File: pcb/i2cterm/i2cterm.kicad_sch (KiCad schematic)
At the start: 8 parts, among them J1 GROVE VERTICAL, J2 GROVE VERTICAL

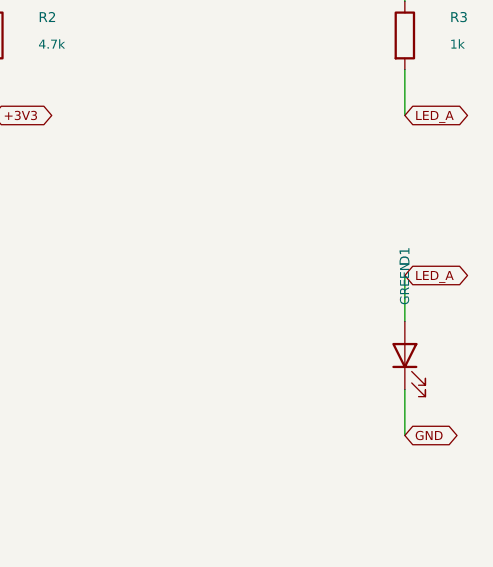
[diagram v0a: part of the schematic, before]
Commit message: Use the basic-library red LED C2286 on the i2cterm board
D1 moves from the extended KT-0603YG green LED (C2289) to the KT-0603R red
LED (C2286), a JLCPCB basic part from the same KENTO 0603 family, which
avoids the extended-part fee. The footprint and the 1k resistor stay; the
current rises from about 1.2 to 1.4 mA. The JLCPCB assembly preview shows
the cathode on the GND pad.

Co-Authored-By: Claude Opus 5.5 <noreply@anthropic.com>
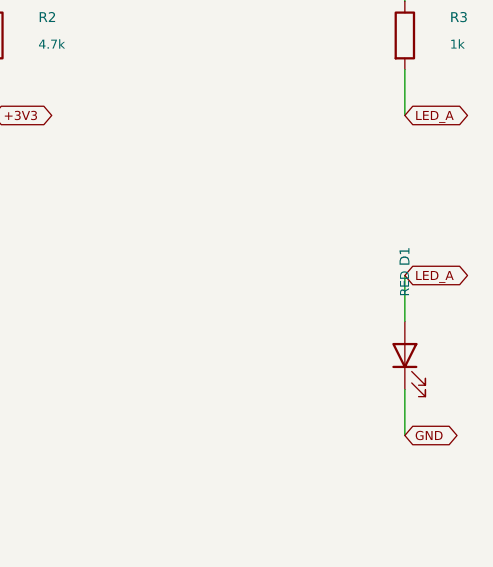
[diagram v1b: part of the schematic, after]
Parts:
- D1: value GREEN -> RED; LCSC C2289 -> C2286; MPN KT-0603YG -> KT-0603R
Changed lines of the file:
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@@
 (wire (pts (xy 185.42 76.2) (xy 185.42 71.12)) (stroke (width 0) (type default)))
 (global_label "LED_A" (shape bidirectional) (at 185.42 71.12 0) (effects (font (size 1.0 1.0)) (justify left)) (property "Intersheetrefs" "${INTERSHEET_REFS}" (at 185.42 71.12 0) (hide yes) (effects (font (size 1.0 1.0)))))
-(symbol (lib_id "Device:LED") (at 185.42 80.01 90) (unit 1) (exclude_from_sim no) (in_bom yes) (on_board yes) (dnp no) (property "Reference" "D1" (at 185.42 69.01 0) (effects (font (size 1.1 1.1)))) (property "Value" "GREEN" (at 185.42 72.01 0) (effects (font (size 1.0 1.0)))) (property "Footprint" "LED_SMD:LED_0603_1608Metric" (at 185.42 80.01 0) (effects (font (size 1.0 1.0))) (hide yes)) (property "Datasheet" "" (at 185.42 80.01 0) (effects (font (size 1.0 1.0))) (hide yes)) (property "Description" "Light emitting diode" (at 185.42 80.01 0) (effects (font (size 1.0 1.0))) (hide yes)) (property "MPN" "KT-0603YG" (at 185.42 80.01 0) (effects (font (size 1.0 1.0))) (hide yes)) (pin "1") (pin "2") (instances (project "i2cterm" (path "/f4c31e8a-4653-5df7-a27a-ec98410162ff" (reference "D1") (unit 1)))) (property "LCSC" "C2289" (at 185.42 80.01 0) (effects (font (size 1 1))) (hide yes)))
+(symbol (lib_id "Device:LED") (at 185.42 80.01 90) (unit 1) (exclude_from_sim no) (in_bom yes) (on_board yes) (dnp no) (property "Reference" "D1" (at 185.42 69.01 0) (effects (font (size 1.1 1.1)))) (property "Value" "RED" (at 185.42 72.01 0) (effects (font (size 1.0 1.0)))) (property "Footprint" "LED_SMD:LED_0603_1608Metric" (at 185.42 80.01 0) (effects (font (size 1.0 1.0))) (hide yes)) (property "Datasheet" "" (at 185.42 80.01 0) (effects (font (size 1.0 1.0))) (hide yes)) (property "Description" "Light emitting diode" (at 185.42 80.01 0) (effects (font (size 1.0 1.0))) (hide yes)) (property "MPN" "KT-0603R" (at 185.42 80.01 0) (effects (font (size 1.0 1.0))) (hide yes)) (pin "1") (pin "2") (instances (project "i2cterm" (path "/f4c31e8a-4653-5df7-a27a-ec98410162ff" (reference "D1") (unit 1)))) (property "LCSC" "C2286" (at 185.42 80.01 0) (effects (font (size 1 1))) (hide yes)))
 (symbol (lib_id "Mechanical:MountingHole") (at 44.45 110.49 0) (unit 1) (exclude_from_sim no) (in_bom no) (on_board yes) (dnp no) (property "Reference" "H1" (at 49.45 108.49 0) (effects (font (size 1.1 1.1)) (justify left))) (property "Value" "M2.5" (at 49.45 111.49 0) (effects (font (size 1.0 1.0)) (justify left))) (property "Footprint" "MountingHole:MountingHole_2.7mm_M2.5" (at 44.45 110.49 0) (effects (font (size 1.0 1.0)) (justify left)) (hide yes)) (property "Datasheet" "" (at 44.45 110.49 0) (effects (font (size 1.0 1.0)) (justify left)) (hide yes)) (property "Description" "Mounting Hole without connection" (at 44.45 110.49 0) (effects (font (size 1.0 1.0)) (justify left)) (hide yes)) (property "MPN" "M2.5 / 2.7mm" (at 44.45 110.49 0) (effects (font (size 1.0 1.0)) (justify left)) (hide yes)) (instances (project "i2cterm" (path "/f4c31e8a-4653-5df7-a27a-ec98410162ff" (reference "H1") (unit 1)))))
 (symbol (lib_id "Mechanical:MountingHole") (at 100.33 110.49 0) (unit 1) (exclude_from_sim no) (in_bom no) (on_board yes) (dnp no) (property "Reference" "H2" (at 105.33 108.49 0) (effects (font (size 1.1 1.1)) (justify left))) (property "Value" "M2.5" (at 105.33 111.49 0) (effects (font (size 1.0 1.0)) (justify left))) (property "Footprint" "MountingHole:MountingHole_2.7mm_M2.5" (at 100.33 110.49 0) (effects (font (size 1.0 1.0)) (justify left)) (hide yes)) (property "Datasheet" "" (at 100.33 110.49 0) (effects (font (size 1.0 1.0)) (justify left)) (hide yes)) (property "Description" "Mounting Hole without connection" (at 100.33 110.49 0) (effects (font (size 1.0 1.0)) (justify left)) (hide yes)) (property "MPN" "M2.5 / 2.7mm" (at 100.33 110.49 0) (effects (font (size 1.0 1.0)) (justify left)) (hide yes)) (instances (project "i2cterm" (path "/f4c31e8a-4653-5df7-a27a-ec98410162ff" (reference "H2") (unit 1)))))
